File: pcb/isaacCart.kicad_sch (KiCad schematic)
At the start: 5 parts, among them J1 CartBus, U1 AT28C256

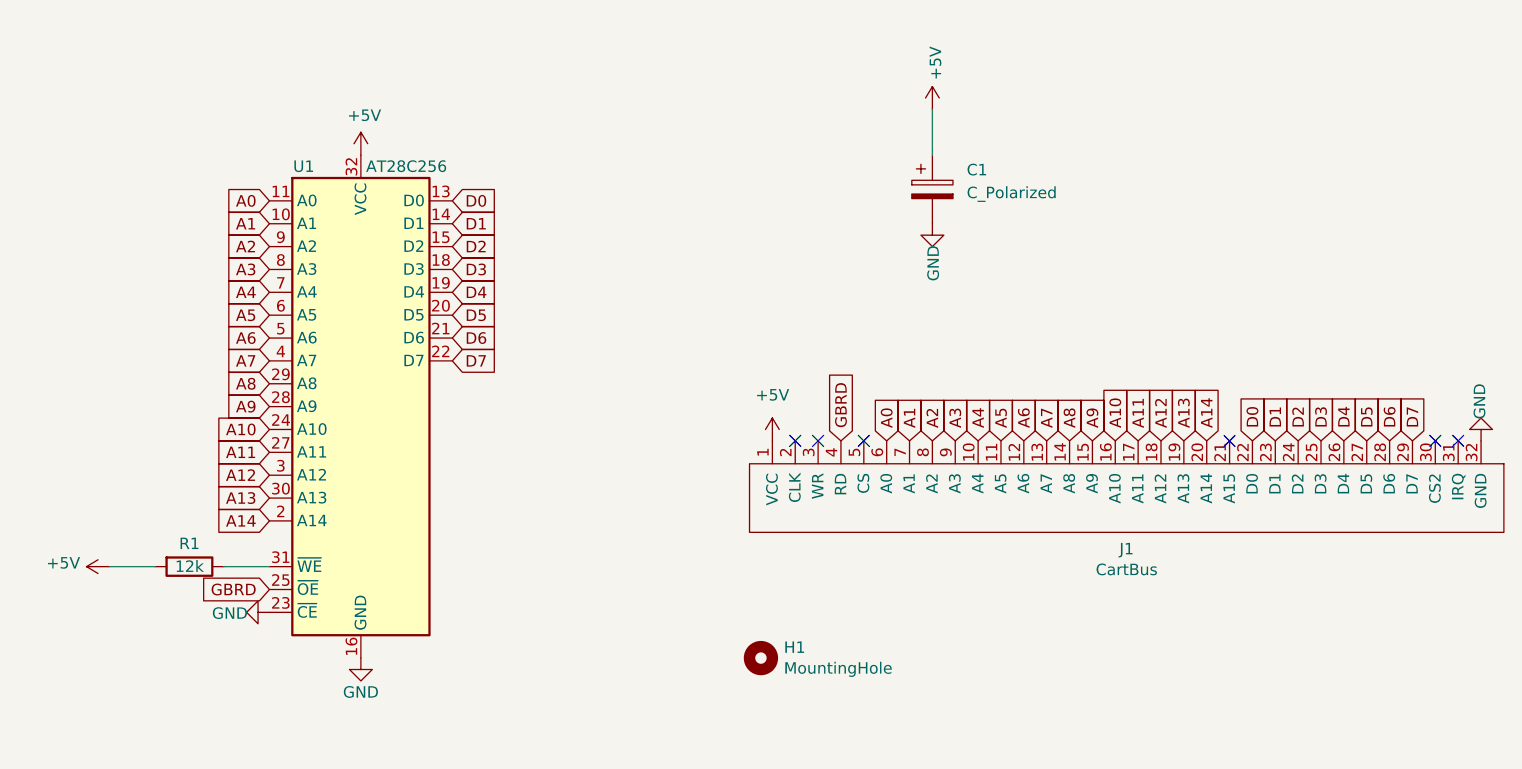
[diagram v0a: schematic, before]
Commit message: New schematic + Board layout based on SST39SF020 PLCC-32 flash chip layout
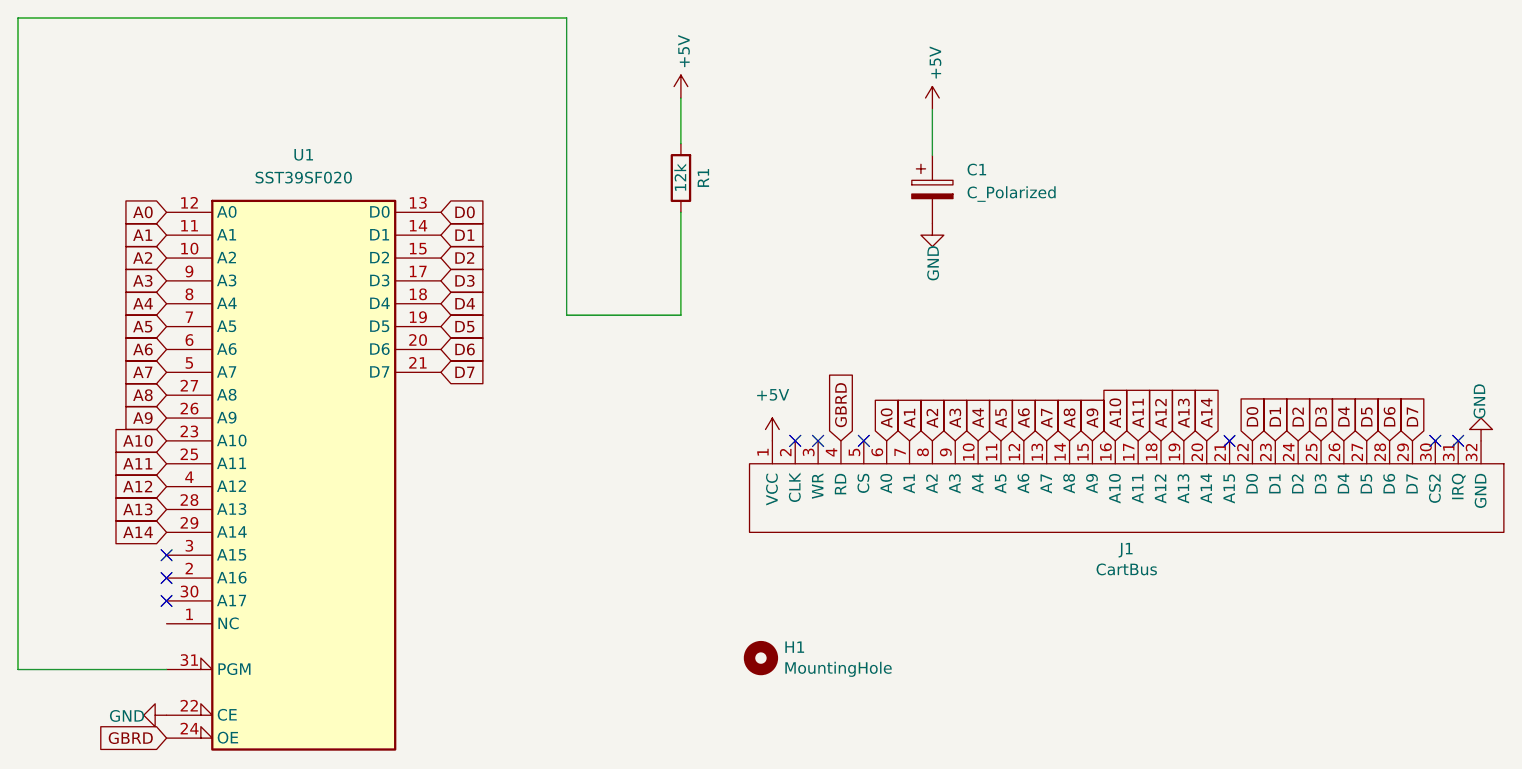
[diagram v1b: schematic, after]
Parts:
- removed U1: AT28C256, GB Cartridge Stuff:PLCC-32_11.4x14.0mm_P1.27mm_SOCKET, symbol Memory_EEPROM:28C256_PLCC
- added U1: SST39SF020, GB Cartridge Stuff:PLCC-32_11.4x14.0mm_P1.27mm_SOCKET, symbol Memory_Flash:SST39SF020
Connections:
- net A0: now also U1.12 (A0)
- net A1: now also U1.11 (A1)
- net A10: now also U1.23 (A10)
- net A11: now also U1.25 (A11)
- net A12: now also U1.4 (A12)
- net A13: now also U1.28 (A13)
- net A14: now also U1.29 (A14)
- net A2: now also U1.10 (A2)
- net A3: now also U1.9 (A3)
- net A4: now also U1.8 (A4)
- net A5: now also U1.7 (A5)
- net A6: now also U1.6 (A6)
- net A7: now also U1.5 (A7)
- net A8: now also U1.27 (A8)
- net A9: now also U1.26 (A9)
- net D0: now also U1.13 (D0)
- net D1: now also U1.14 (D1)
- net D2: now also U1.15 (D2)
- net D3: now also U1.17 (D3)
- net D4: now also U1.18 (D4)
- net D5: now also U1.19 (D5)
- net D6: now also U1.20 (D6)
- net D7: now also U1.21 (D7)
- net GBRD: now also U1.24 (OE)
- net GND: now also U1.16 (GND), U1.22 (CE)
- net at R1.1: now also U1.31 (PGM)
- new net VCC: U1.32 (VCC)
- no-connect marks 6 -> 9
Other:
- company: Isaac.Flaum -> Flashable DMG cartridge for games with no mapper
- title: Isaac Cart -> Isaac Cart 2
- moved on the sheet: R1
